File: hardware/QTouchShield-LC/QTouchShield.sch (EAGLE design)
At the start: 59 parts, among them IC1 AT32UC3C0512CJEDEC-MS-026, J1 SNS00...07, J10 CAPS08...15, J11 CAPS16...23, J12 CAPS24...31, J2 SNS08...15, J3 SNS16...23, J4 SNS24...31, J5 RES00...07, J6 RES08...15, J7 RES16...23, J8 RES24...31, J9 CAPS00...07, U1 ARDUINO-2560-MEGA-R3-SMD

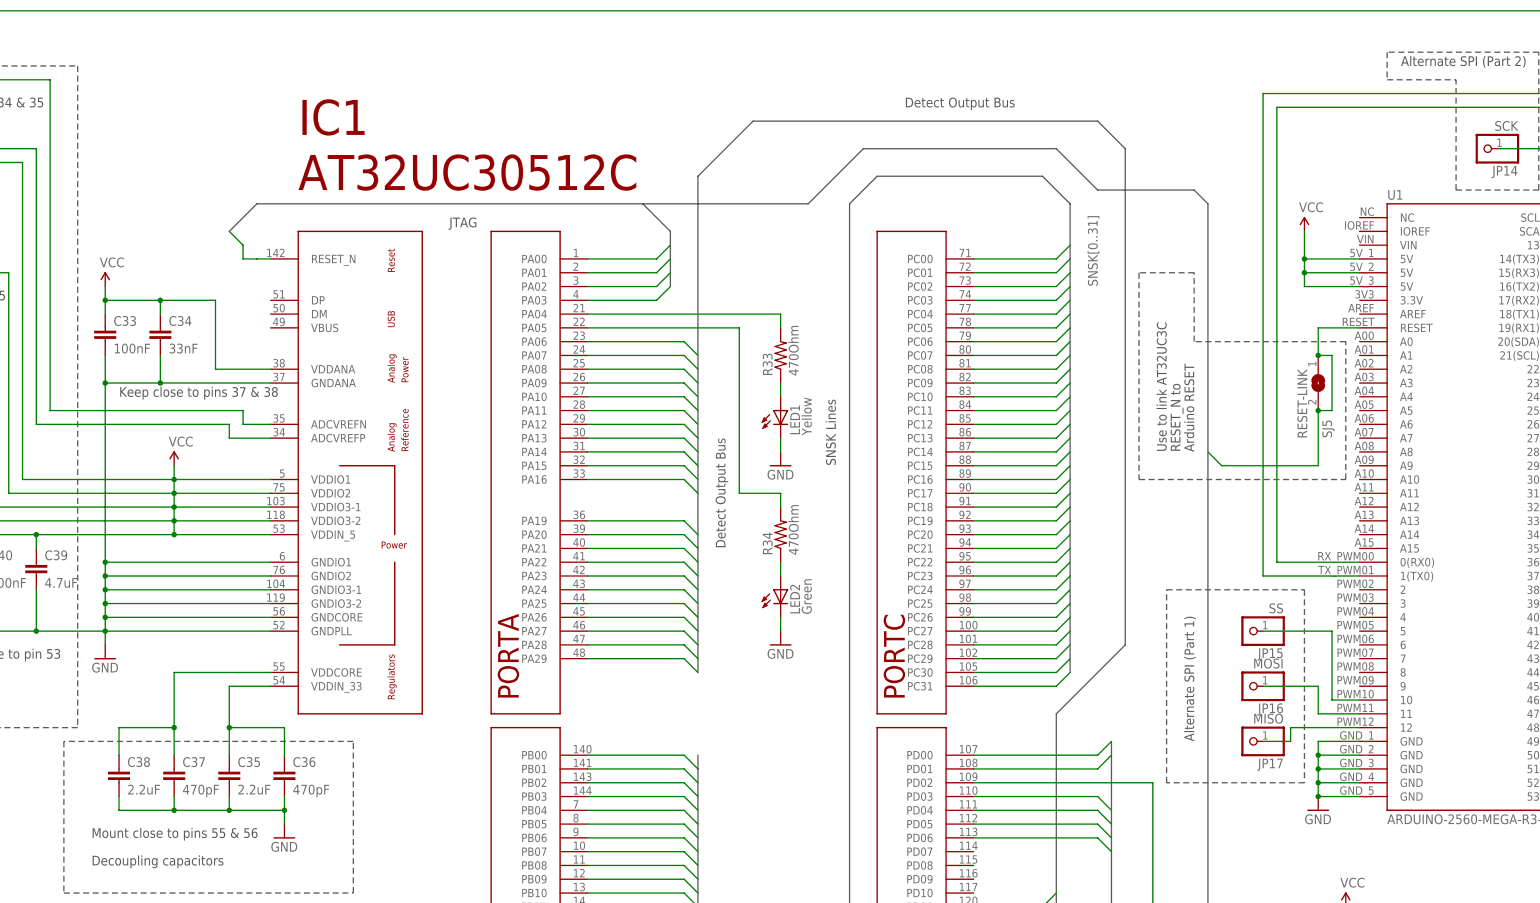
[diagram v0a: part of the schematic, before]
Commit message: Added USB Connector (B-Large) for firmware updates.
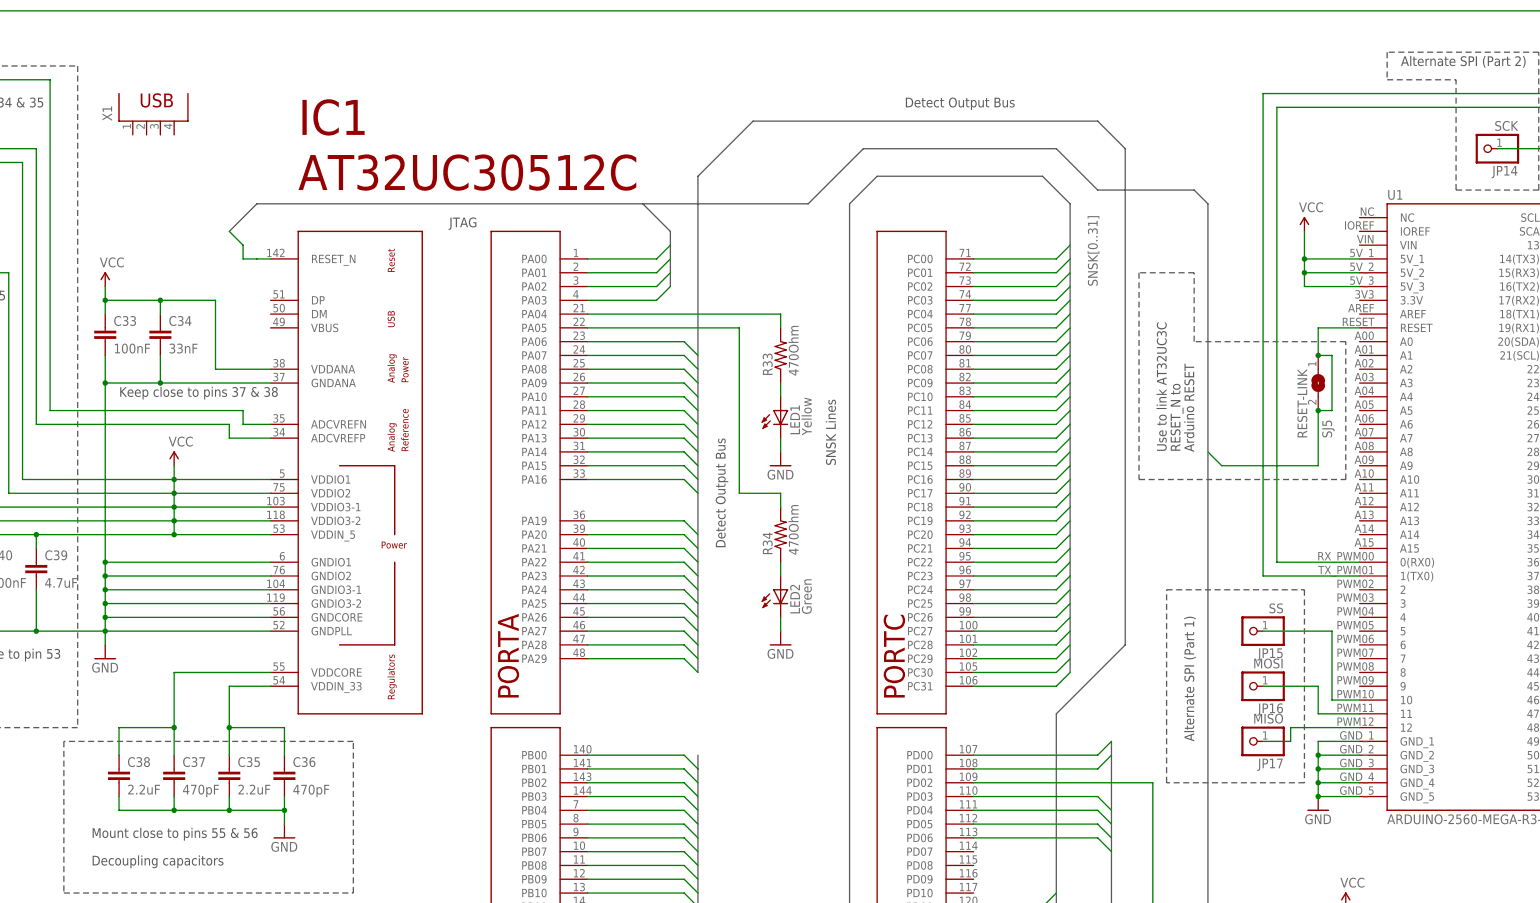
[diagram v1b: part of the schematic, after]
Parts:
- added X1: (no value), con-berg:PN87520
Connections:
- net GND: now also U1.GND_1, U1.GND_2, U1.GND_3, U1.GND_4, U1.GND_5; no longer U1.GND@0, U1.GND@1, U1.GND@2, U1.GND@3, U1.GND@4
- net VCC: now also U1.5V_1, U1.5V_2, U1.5V_3; no longer U1.5V@0, U1.5V@1, U1.5V@2
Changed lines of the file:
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@@
 <part name="J6" library="codinghead" deviceset="2X8-HEADER" device="" technology="SMD" value="RES08...15"/>
 <part name="J5" library="codinghead" deviceset="2X8-HEADER" device="" technology="SMD" value="RES00...07"/>
+<part name="X1" library="con-berg" deviceset="PN87520" device=""/>
 </parts>
 <sheets>
@@
 <instance part="J6" gate="A" x="208.28" y="-187.96" rot="R270"/>
 <instance part="J5" gate="A" x="246.38" y="-187.96" rot="R270"/>
+<instance part="X1" gate="G$1" x="-15.24" y="86.36" rot="R90"/>
 </instances>
 <busses>
@@
 <segment>
 <pinref part="GND6" gate="1" pin="GND"/>
-<pinref part="U1" gate="A" pin="GND@0"/>
+<pinref part="U1" gate="A" pin="GND_1"/>
 <wire x1="198.12" y1="-27.94" x2="198.12" y2="-30.48" width="0.1524" layer="91"/>
 <wire x1="198.12" y1="-30.48" x2="198.12" y2="-33.02" width="0.1524" layer="91"/>
@@
 <wire x1="198.12" y1="-35.56" x2="198.12" y2="-38.1" width="0.1524" layer="91"/>
 <wire x1="205.74" y1="-27.94" x2="198.12" y2="-27.94" width="0.1524" layer="91"/>
-<pinref part="U1" gate="A" pin="GND@1"/>
+<pinref part="U1" gate="A" pin="GND_2"/>
 <wire x1="205.74" y1="-30.48" x2="198.12" y2="-30.48" width="0.1524" layer="91"/>
 <junction x="198.12" y="-30.48"/>
-<pinref part="U1" gate="A" pin="GND@2"/>
+<pinref part="U1" gate="A" pin="GND_3"/>
 <wire x1="205.74" y1="-33.02" x2="198.12" y2="-33.02" width="0.1524" layer="91"/>
 <junction x="198.12" y="-33.02"/>
-<pinref part="U1" gate="A" pin="GND@3"/>
+<pinref part="U1" gate="A" pin="GND_4"/>
 <wire x1="205.74" y1="-35.56" x2="198.12" y2="-35.56" width="0.1524" layer="91"/>
 <junction x="198.12" y="-35.56"/>
-<pinref part="U1" gate="A" pin="GND@4"/>
+<pinref part="U1" gate="A" pin="GND_5"/>
 <wire x1="205.74" y1="-38.1" x2="198.12" y2="-38.1" width="0.1524" layer="91"/>
 <junction x="198.12" y="-38.1"/>
@@
 </segment>
 <segment>
-<pinref part="U1" gate="A" pin="5V@0"/>
+<pinref part="U1" gate="A" pin="5V_1"/>
 <wire x1="205.74" y1="60.96" x2="195.58" y2="60.96" width="0.1524" layer="91"/>
 <pinref part="P+3" gate="1" pin="VCC"/>
@@
 <wire x1="195.58" y1="60.96" x2="195.58" y2="58.42" width="0.1524" layer="91"/>
 <junction x="195.58" y="60.96"/>
-<pinref part="U1" gate="A" pin="5V@1"/>
+<pinref part="U1" gate="A" pin="5V_2"/>
 <wire x1="195.58" y1="58.42" x2="205.74" y2="58.42" width="0.1524" layer="91"/>
 <wire x1="195.58" y1="58.42" x2="195.58" y2="55.88" width="0.1524" layer="91"/>
 <junction x="195.58" y="58.42"/>
-<pinref part="U1" gate="A" pin="5V@2"/>
+<pinref part="U1" gate="A" pin="5V_3"/>
 <wire x1="195.58" y1="55.88" x2="205.74" y2="55.88" width="0.1524" layer="91"/>
 </segment>

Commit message: Major update to LC version of shield.
Major update to shield design including:
- Moving headers to surface mount technology
- Including level shifters for SPI and USART i/f
- USB connector for firmware flash upgrade (not yet complete)
- Jumper system for selecting MEGA or UNO style SPI interface
- Plus other tidying up
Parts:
- removed JP10, JP15: SS, pinhead:PINHD-1X1
- removed JP11, JP14: SCK, pinhead:PINHD-1X1
- removed JP12, JP17: MISO, pinhead:PINHD-1X1
- removed JP13, JP16: MOSI, pinhead:PINHD-1X1
- removed SJ1, SJ2, SJ3, SJ4: (no value), jumper:SJ
- removed U$1, U$2: 2X8-HEADERSMD, codinghead:2X8-HEADERSMD
- added J13: SPI-MEGA, codinghead:2X4-HEADERSMT-MALE
- added J14: SPI-UNO, codinghead:2X4-HEADERSMT-MALE
- added J16: DETECT00...15, codinghead:2X8-HEADERHARWIN-PIN-SMT
- added J17: DETECT16...31, codinghead:2X8-HEADERHARWIN-PIN-SMT
- added Q1, Q2, Q3, Q4, Q5, Q6: BSS138, SparkFun:MOSFET-NCHANNELSMD
- J1, J2, J3, J4: device codinghead:2X8-HEADERSMD -> codinghead:2X8-HEADERHARWIN-PIN-SMT
- J10, J11, J12, J5, J6, J7, J8, J9: device codinghead:2X8-HEADERSMD -> codinghead:2X8-HEADERHARWIN-RECEPTACLE-SMT
- renumbered JP9 to J15
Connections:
- new net ADT-SPI0-MISO: J13.2, J14.2, Q3.S
- new net ADT-SPI0-MOSI: J13.4, J14.4, Q4.S
- new net ADT-SPI0-SCK: J13.6, J14.6, Q2.S
- new net ADT-SPI0-SS: J13.8, J14.8, Q1.S
- new net ADT-USART0-RXD: J15.12, J15.16, J15.4, J15.8, Q5.S
- new net ADT-USART0-TXD: J15.10, J15.14, J15.2, J15.6, Q6.S
- new net IOREF: Q1.G, Q2.G, Q3.G, Q4.G, Q5.G, Q6.G, U1.IOREF
- new net MISO-MEGA: J13.1, U1.50
- new net MOSI-MEGA: J13.3, U1.51
- new net N$34: IC1.DP, X1.3
- new net N$35: IC1.DM, X1.2
- new net SCK-MEGA: J13.5, U1.52
- new net SS-MEGA: J13.7, U1.53
- net GND: now also X1.4
- net SDT-SPI0-MISO: now also Q3.D; no longer JP12.1, SJ4.1, SJ4.2, U1.50
- net SDT-SPI0-MOSI: now also Q4.D; no longer JP13.1, SJ3.1, SJ3.2, U1.51
- net SDT-SPI0-SCK: now also Q2.D; no longer JP11.1, SJ2.1, SJ2.2, U1.52
- net SDT-SPI0-SS: now also Q1.D; no longer JP10.1, SJ1.1, SJ1.2, U1.53
- net SDT-USART0-RXD: now also Q6.D; no longer J15.12, J15.16, J15.4, J15.8
- net SDT-USART0-TXD: now also Q5.D; no longer J15.10, J15.14, J15.2, J15.6
- net SHIELD-DETECT0: now also J16.1; no longer U$1.1
- net SHIELD-DETECT1: now also J16.2; no longer U$1.2
- net SHIELD-DETECT10: now also J16.11; no longer U$1.11
- net SHIELD-DETECT11: now also J16.12; no longer U$1.12
- net SHIELD-DETECT12: now also J16.13; no longer U$1.13
- net SHIELD-DETECT13: now also J16.14; no longer U$1.14
- net SHIELD-DETECT14: now also J16.15; no longer U$1.15
- net SHIELD-DETECT15: now also J16.16; no longer U$1.16
- net SHIELD-DETECT16: now also J17.1; no longer U$2.1
- net SHIELD-DETECT17: now also J17.2; no longer U$2.2
- net SHIELD-DETECT18: now also J17.3; no longer U$2.3
- net SHIELD-DETECT19: now also J17.4; no longer U$2.4
- net SHIELD-DETECT2: now also J16.3; no longer U$1.3
- net SHIELD-DETECT20: now also J17.5; no longer U$2.5
- net SHIELD-DETECT21: now also J17.6; no longer U$2.6
- net SHIELD-DETECT22: now also J17.7; no longer U$2.7
- net SHIELD-DETECT23: now also J17.8; no longer U$2.8
- net SHIELD-DETECT24: now also J17.9; no longer U$2.9
- net SHIELD-DETECT25: now also J17.10; no longer U$2.10
- net SHIELD-DETECT26: now also J17.11; no longer U$2.11
- net SHIELD-DETECT27: now also J17.12; no longer U$2.12
- net SHIELD-DETECT28: now also J17.13; no longer U$2.13
- net SHIELD-DETECT29: now also J17.14; no longer U$2.14
- net SHIELD-DETECT3: now also J16.4; no longer U$1.4
- net SHIELD-DETECT30: now also J17.15; no longer U$2.15
- net SHIELD-DETECT31: now also J17.16; no longer U$2.16
- net SHIELD-DETECT4: now also J16.5; no longer U$1.5
- net SHIELD-DETECT5: now also J16.6; no longer U$1.6
- net SHIELD-DETECT6: now also J16.7; no longer U$1.7
- net SHIELD-DETECT7: now also J16.8; no longer U$1.8
- net SHIELD-DETECT8: now also J16.9; no longer U$1.9
- net SHIELD-DETECT9: now also J16.10; no longer U$1.10
- net SPI-MISO-ALT: now also J14.1; no longer JP17.1
- net SPI-MOSI-ALT: now also J14.3; no longer JP16.1
- net SPI-SCK-ALT: now also J14.5; no longer JP14.1
- net SPI-SS-ALT: now also J14.7; no longer JP15.1
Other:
- note added: "(Only req. when"
- note added: "(instead of SPI)"
- note added: "Arduino is *not*"
- note added: "Board"
- note added: "Choose either MEGA or UNO"
- note added: "Debug Bit-Bang"
- note added: "Detection"
- note added: "Interface to"
- note added: "Level Shifter"
- note added: "Outputs"
- note added: "QT600 Bit-Banged SPI Debug Interface"
- note added: "QT600 Interface"
- note added: "SPI interface"
- note added: "SPI/USART"
- note added: "USB Firmware Update B-Receptacle"
- note added: "present)"
- note removed: "(Only req. when Arduino"
- note removed: "Alternate SPI (Part 1)"
- note removed: "Alternate SPI (Part 2)"
- note removed: "Cut wires to use"
- note removed: "Detection Logic Outputs"
- note removed: "One pin per "channel""
- note removed: "SPI-COMS"
- note removed: "alternative SPI"
- note removed: "interface"
- note removed: "is *not* present)"
- moved on the sheet: IC1, JP1

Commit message: Another attempt, more successful, at routingh the board!
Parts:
- removed JP18: TOUCH DATA, pinhead:PINHD-2X5
- removed JP6: JTAG, pinhead:PINHD-2X5
- added J18: JTAG, codinghead:2X5-HEADERTHRU-HOLE
- added J19: TOUCH DATA, codinghead:2X5-HEADERTHRU-HOLE
- J11: value CAPS16...23 -> CAPS24...31
- J12: value CAPS24...31 -> CAPS16...23
- X1: value (none) -> Firmware Upgrade Port
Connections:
- net GND: now also J18.10, J18.2, J19.9; no longer JP18.9, JP6.10, JP6.2
- net JTAG_RESET: now also J18.6; no longer JP6.6
- net JTAG_TCK: now also J18.1; no longer JP6.1
- net JTAG_TDI: now also J18.9; no longer JP6.9
- net JTAG_TDO: now also J18.3; no longer JP6.3
- net JTAG_TMS: now also J18.5; no longer JP6.5
- net SNS16: now also J12.15; no longer J11.1
- net SNS17: now also J12.13; no longer J11.3
- net SNS18: now also J12.11; no longer J11.5
- net SNS19: now also J12.9; no longer J11.7
- net SNS20: now also J12.7; no longer J11.9
- net SNS21: now also J12.5; no longer J11.11
- net SNS22: now also J12.3; no longer J11.13
- net SNS23: now also J12.1; no longer J11.15
- net SNS24: now also J11.15; no longer J12.1
- net SNS25: now also J11.13; no longer J12.3
- net SNS26: now also J11.11; no longer J12.5
- net SNS27: now also J11.9; no longer J12.7
- net SNS28: now also J11.7; no longer J12.9
- net SNS29: now also J11.5; no longer J12.11
- net SNS30: now also J11.3; no longer J12.13
- net SNS31: now also J11.1; no longer J12.15
- net SNSK29: no longer J8.13
- net SNSK30: now also J8.13
- net TOUCH_DATA-MISO: now also J19.7; no longer JP18.7
- net TOUCH_DATA-MOSI: now also J19.6; no longer JP18.6
- net TOUCH_DATA-SCK: now also J19.8; no longer JP18.8
- net TOUCH_DATA-SS: now also J19.5; no longer JP18.5
- net VCC: now also J18.4, J19.10; no longer JP18.10, JP6.4

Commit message: 95% complete routing of board; extra VCC decoupling; USB changes.
Routing about 95% complete.
Added extra 10uF cap in the VCC supply.
Added in-line resistors in the D+/D- lines.
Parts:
- added C1: 10uF/35V, SparkFun:CAP_POLC
- added R1, R2: 39R, SparkFun:RESISTOR0805-RES
- J15: device pinhead:PINHD-2X8 -> codinghead:2X8-HEADERHARWIN-PIN-SMT
- J18, J19: device codinghead:2X5-HEADERTHRU-HOLE -> codinghead:2X5-HEADERSMT
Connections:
- new net USB-DM: IC1.DM, R1.1
- new net USB-DP: IC1.DP, R2.1
- net GND: now also C1.-; no longer U1.GND_2, U1.GND_3, U1.GND_4, U1.GND_5
- net N$34: now also R1.2, X1.2; no longer IC1.DP, X1.3
- net N$35: now also R2.2, X1.3; no longer IC1.DM, X1.2
- net SHIELD-DETECT16: now also J17.15; no longer J17.1
- net SHIELD-DETECT17: now also J17.16; no longer J17.2
- net SHIELD-DETECT18: now also J17.13; no longer J17.3
- net SHIELD-DETECT19: now also J17.14; no longer J17.4
- net SHIELD-DETECT20: now also J17.11; no longer J17.5
- net SHIELD-DETECT21: now also J17.12; no longer J17.6
- net SHIELD-DETECT22: now also J17.9; no longer J17.7
- net SHIELD-DETECT23: now also J17.10; no longer J17.8
- net SHIELD-DETECT24: now also J17.7; no longer J17.9
- net SHIELD-DETECT25: now also J17.8; no longer J17.10
- net SHIELD-DETECT26: now also J17.5; no longer J17.11
- net SHIELD-DETECT27: now also J17.6; no longer J17.12
- net SHIELD-DETECT28: now also J17.3; no longer J17.13
- net SHIELD-DETECT29: now also J17.4; no longer J17.14
- net SHIELD-DETECT30: now also J17.1; no longer J17.15
- net SHIELD-DETECT31: now also J17.2; no longer J17.16
- net VCC: now also C1.+; no longer U1.5V_2, U1.5V_3
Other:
- note added: "! Single point of GND only !"
- note added: "! Single point of VCC 5V only !"
- note added: "5V_1 of Arduino"
- note added: "Keep close to pin"
- moved on the sheet: C42, C43, C44

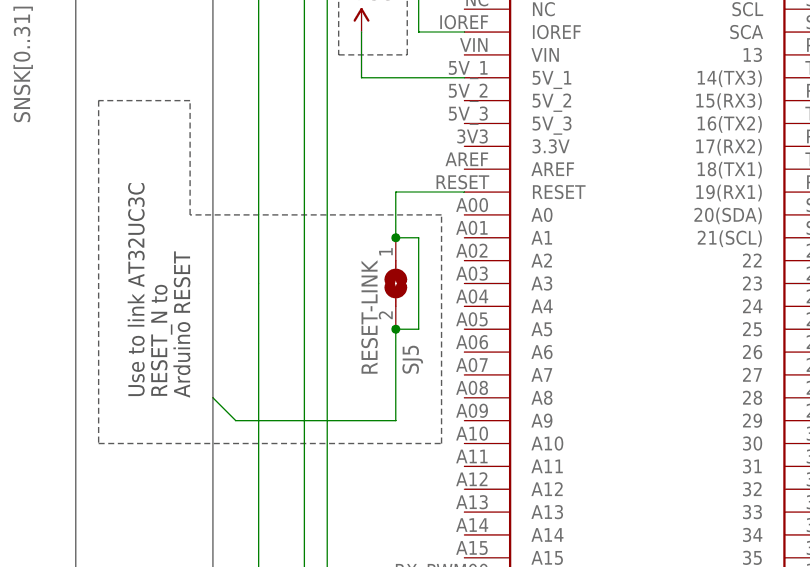
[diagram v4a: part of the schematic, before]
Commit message: Split Arduino reset electrically from UC3 & JTAG reset signals.
Split resets. If user wants to reset Arduino from switch, they have to
solder blob the jumper by hand.
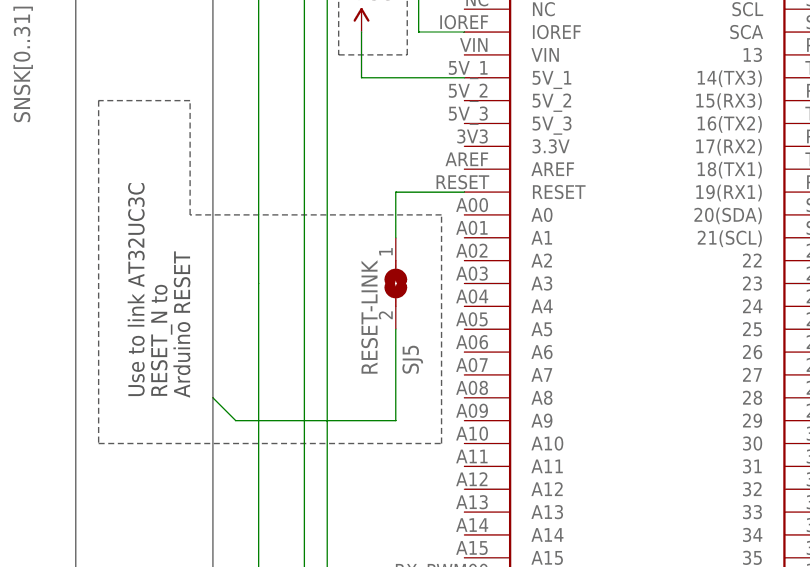
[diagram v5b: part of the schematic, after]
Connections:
- new net ARDUINO_RESET: SJ5.1, U1.RESET
- net JTAG_RESET: no longer SJ5.1, U1.RESET
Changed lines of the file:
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@@
 <pinref part="SJ5" gate="1" pin="2"/>
 <wire x1="198.12" y1="22.86" x2="198.12" y2="33.02" width="0.1524" layer="91"/>
-<wire x1="198.12" y1="33.02" x2="200.66" y2="33.02" width="0.1524" layer="91"/>
-<junction x="198.12" y="33.02"/>
-<wire x1="200.66" y1="33.02" x2="200.66" y2="43.18" width="0.1524" layer="91"/>
-<pinref part="SJ5" gate="1" pin="1"/>
-<wire x1="198.12" y1="43.18" x2="198.12" y2="48.26" width="0.1524" layer="91"/>
-<pinref part="U1" gate="A" pin="RESET"/>
-<wire x1="198.12" y1="48.26" x2="205.74" y2="48.26" width="0.1524" layer="91"/>
-<wire x1="200.66" y1="43.18" x2="198.12" y2="43.18" width="0.1524" layer="91"/>
-<junction x="198.12" y="43.18"/>
 </segment>
 </net>
@@
 </segment>
 </net>
+<net name="ARDUINO_RESET" class="0">
+<segment>
+<pinref part="U1" gate="A" pin="RESET"/>
+<pinref part="SJ5" gate="1" pin="1"/>
+<wire x1="198.12" y1="43.18" x2="198.12" y2="48.26" width="0.1524" layer="91"/>
+<wire x1="198.12" y1="48.26" x2="205.74" y2="48.26" width="0.1524" layer="91"/>
+</segment>
+</net>
